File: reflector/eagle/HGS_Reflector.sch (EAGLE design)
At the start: 19 parts, among them J1 U.FL, U1 TQP3M9037, U2 TQP3M903X, U3 LP2985XX-N

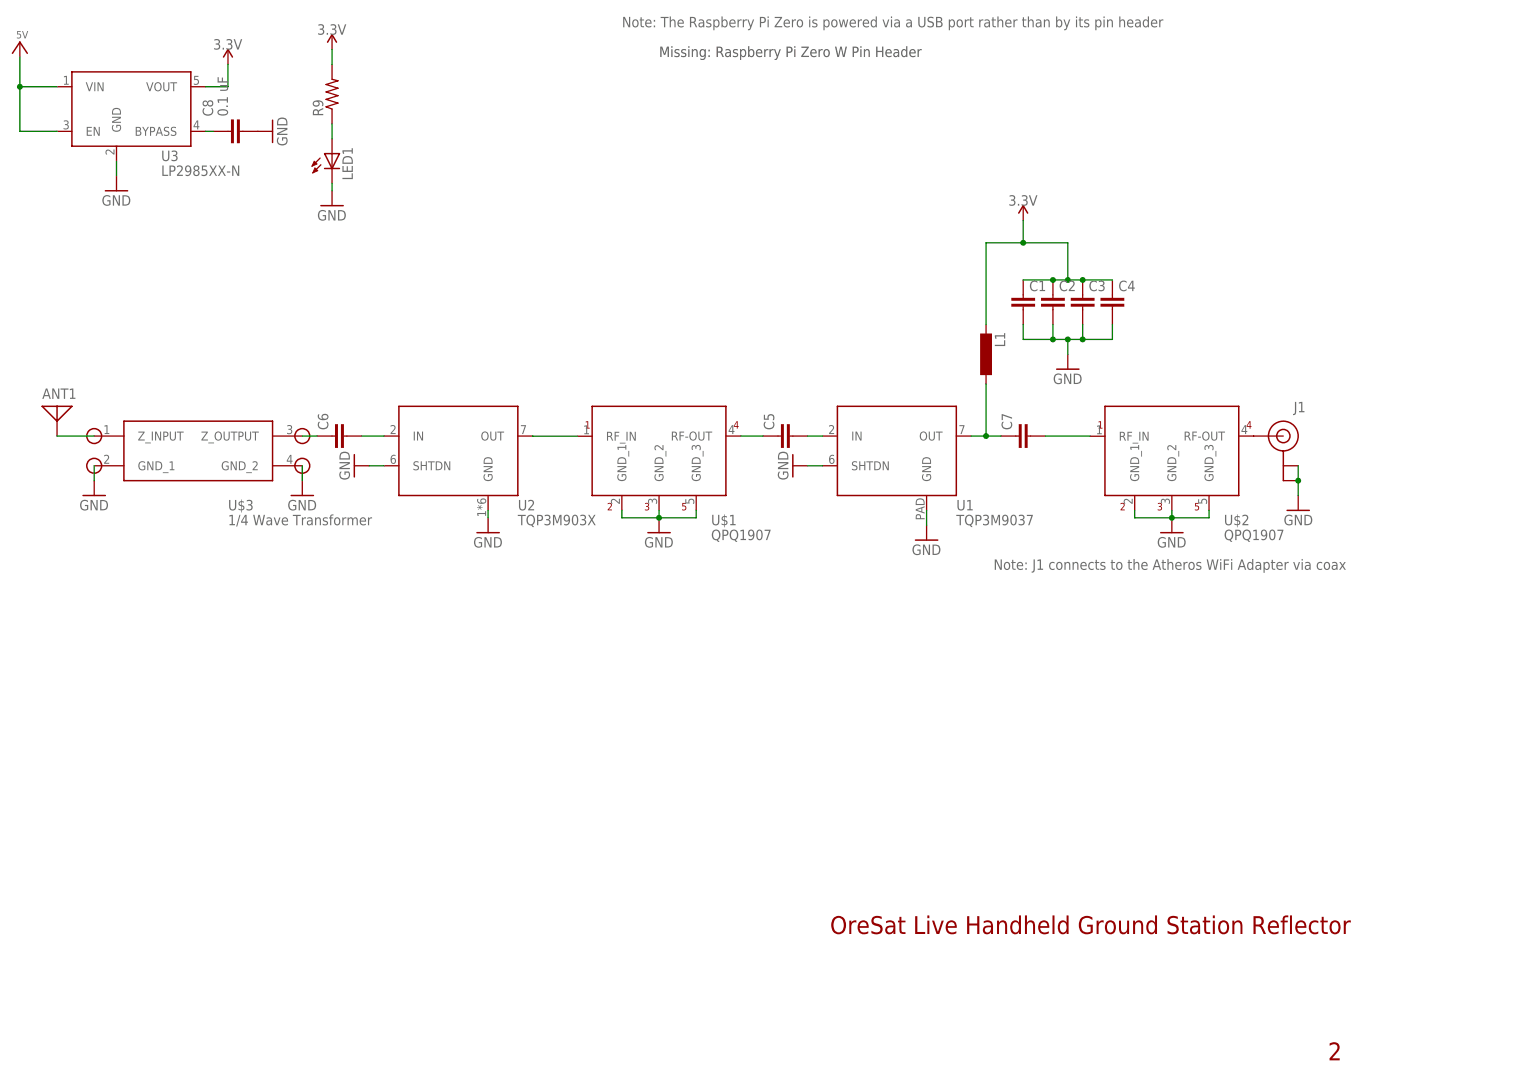
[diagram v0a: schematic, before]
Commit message: My EAGLE accidentally named something wrong, so I am fixing that.
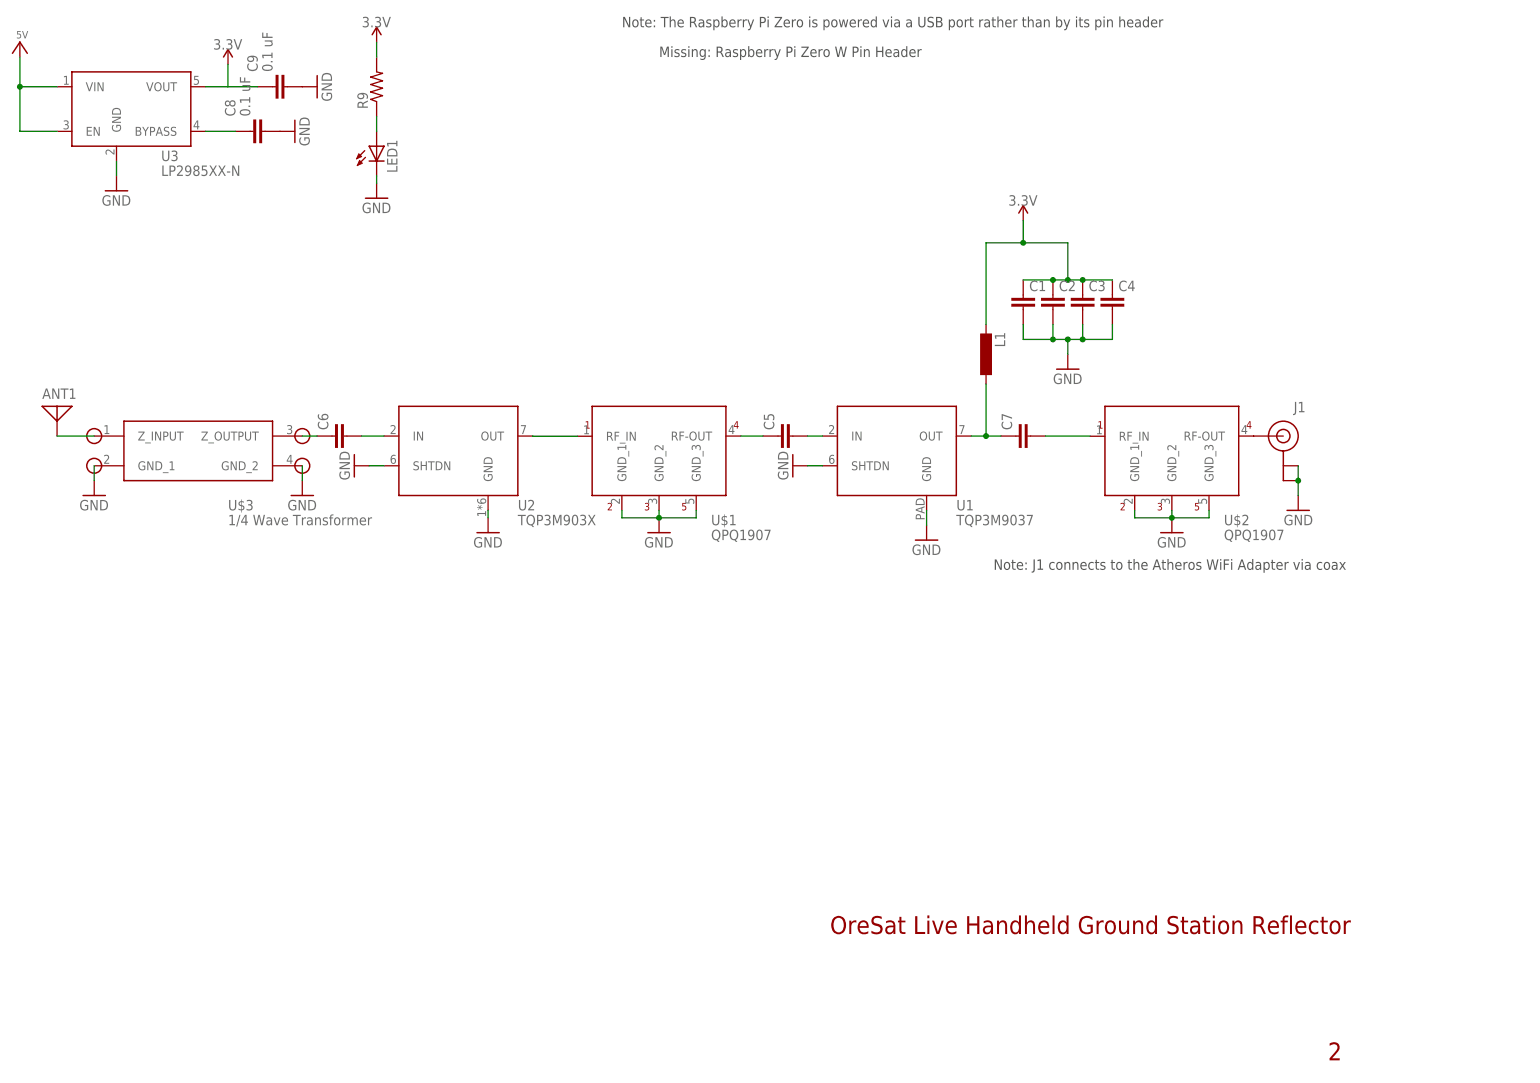
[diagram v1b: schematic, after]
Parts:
- added C9: 0.1 uF, ngspice-simulation:C
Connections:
- new net N$13: C9.1, U3.VOUT
- net 3.3V: no longer U3.VOUT
- net GND: now also C9.2
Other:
- moved on the sheet: C8, LED1, R9
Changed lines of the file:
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@@
 <part name="C8" library="ngspice-simulation" library_urn="urn:adsk.eagle:library:527439" deviceset="C" device="" value="0.1 uF"/>
 <part name="GND13" library="supply1" library_urn="urn:adsk.eagle:library:371" deviceset="GND" device=""/>
+<part name="C9" library="ngspice-simulation" library_urn="urn:adsk.eagle:library:527439" deviceset="C" device="" value="0.1 uF"/>
+<part name="GND14" library="supply1" library_urn="urn:adsk.eagle:library:371" deviceset="GND" device=""/>
 </parts>
 <sheets>
@@
 <text x="180.34" y="27.94" size="3.048" layer="94">OreSat Live Handheld Ground Station Reflector</text>
 <text x="265.43" y="6.35" size="3.048" layer="94">2</text>
-<text x="144.78" y="182.88" size="1.778" layer="95">Note: The Raspberry Pi Zero is powered via a USB port rather than by its pin header</text>
-<text x="208.28" y="90.17" size="1.778" layer="95">Note: J1 connects to the Atheros WiFi Adapter via coax</text>
+<text x="144.78" y="182.88" size="1.778" layer="97">Note: The Raspberry Pi Zero is powered via a USB port rather than by its pin header</text>
+<text x="208.28" y="90.17" size="1.778" layer="97">Note: J1 connects to the Atheros WiFi Adapter via coax</text>
 </plain>
 <instances>
@@
 <attribute name="VALUE" x="218.44" y="121.92" size="1.778" layer="96"/>
 </instance>
-<instance part="LED1" gate="G$1" x="95.25" y="161.29" smashed="yes">
-<attribute name="NAME" x="98.806" y="156.718" size="1.778" layer="95" rot="R90"/>
-<attribute name="VALUE" x="100.965" y="156.718" size="1.778" layer="96" rot="R90"/>
-</instance>
-<instance part="R9" gate="R" x="95.25" y="171.45" smashed="yes" rot="R90">
-<attribute name="NAME" x="93.7514" y="167.64" size="1.778" layer="95" rot="R90"/>
-<attribute name="VALUE" x="98.552" y="167.64" size="1.778" layer="96" rot="R90"/>
+<instance part="LED1" gate="G$1" x="102.87" y="162.56" smashed="yes">
+<attribute name="NAME" x="106.426" y="157.988" size="1.778" layer="95" rot="R90"/>
+<attribute name="VALUE" x="108.585" y="157.988" size="1.778" layer="96" rot="R90"/>
+</instance>
+<instance part="R9" gate="R" x="102.87" y="172.72" smashed="yes" rot="R90">
+<attribute name="NAME" x="101.3714" y="168.91" size="1.778" layer="95" rot="R90"/>
+<attribute name="VALUE" x="106.172" y="168.91" size="1.778" layer="96" rot="R90"/>
 </instance>
 <instance part="C1" gate="CE" x="213.36" y="137.16" smashed="yes">
@@
 <attribute name="VALUE" x="119.38" y="93.98" size="1.778" layer="96"/>
 </instance>
-<instance part="3.3V2" gate="G$1" x="95.25" y="181.61" smashed="yes">
-<attribute name="VALUE" x="92.71" y="181.61" size="1.778" layer="96"/>
-</instance>
-<instance part="GND6" gate="1" x="95.25" y="152.4" smashed="yes">
-<attribute name="VALUE" x="92.71" y="149.86" size="1.778" layer="96"/>
+<instance part="3.3V2" gate="G$1" x="102.87" y="182.88" smashed="yes">
+<attribute name="VALUE" x="100.33" y="182.88" size="1.778" layer="96"/>
+</instance>
+<instance part="GND6" gate="1" x="102.87" y="153.67" smashed="yes">
+<attribute name="VALUE" x="100.33" y="151.13" size="1.778" layer="96"/>
 </instance>
 <instance part="C6" gate="CE" x="95.25" y="113.03" smashed="yes" rot="R90">
@@
 <attribute name="VALUE" x="171.45" y="110.49" size="1.778" layer="96" rot="R270"/>
 </instance>
-<instance part="C8" gate="G$1" x="77.47" y="165.1" smashed="yes" rot="R90">
-<attribute name="NAME" x="74.93" y="167.64" size="1.778" layer="95" rot="R90"/>
-<attribute name="VALUE" x="77.47" y="167.64" size="1.778" layer="96" rot="R90"/>
-</instance>
-<instance part="GND13" gate="1" x="85.09" y="165.1" smashed="yes" rot="R90">
-<attribute name="VALUE" x="87.63" y="162.56" size="1.778" layer="96" rot="R90"/>
+<instance part="C8" gate="G$1" x="81.28" y="165.1" smashed="yes" rot="R90">
+<attribute name="NAME" x="78.74" y="167.64" size="1.778" layer="95" rot="R90"/>
+<attribute name="VALUE" x="81.28" y="167.64" size="1.778" layer="96" rot="R90"/>
+</instance>
+<instance part="GND13" gate="1" x="88.9" y="165.1" smashed="yes" rot="R90">
+<attribute name="VALUE" x="91.44" y="162.56" size="1.778" layer="96" rot="R90"/>
+</instance>
+<instance part="C9" gate="G$1" x="85.09" y="172.72" smashed="yes" rot="R90">
+<attribute name="NAME" x="82.55" y="175.26" size="1.778" layer="95" rot="R90"/>
+<attribute name="VALUE" x="85.09" y="175.26" size="1.778" layer="96" rot="R90"/>
+</instance>
+<instance part="GND14" gate="1" x="92.71" y="172.72" smashed="yes" rot="R90">
+<attribute name="VALUE" x="95.25" y="170.18" size="1.778" layer="96" rot="R90"/>
 </instance>
 </instances>
@@
 <pinref part="LED1" gate="G$1" pin="C"/>
 <pinref part="GND6" gate="1" pin="GND"/>
-<wire x1="95.25" y1="154.94" x2="95.25" y2="156.21" width="0.1524" layer="91"/>
+<wire x1="102.87" y1="156.21" x2="102.87" y2="157.48" width="0.1524" layer="91"/>
 </segment>
 <segment>
@@
 <pinref part="GND13" gate="1" pin="GND"/>
 </segment>
+<segment>
+<pinref part="C9" gate="G$1" pin="2"/>
+<pinref part="GND14" gate="1" pin="GND"/>
+</segment>
 </net>
 <net name="N$5" class="0">
@@
 <pinref part="LED1" gate="G$1" pin="A"/>
 <pinref part="R9" gate="R" pin="1"/>
-<wire x1="95.25" y1="166.37" x2="95.25" y2="163.83" width="0.1524" layer="91"/>
+<wire x1="102.87" y1="167.64" x2="102.87" y2="165.1" width="0.1524" layer="91"/>
 </segment>
 </net>
 <net name="3.3V" class="0">
-<segment>
-<pinref part="U3" gate="G$1" pin="VOUT"/>
-<pinref part="3.3V1" gate="G$1" pin="3.3V"/>
-<wire x1="73.66" y1="172.72" x2="77.47" y2="172.72" width="0.1524" layer="91"/>
-<wire x1="77.47" y1="172.72" x2="77.47" y2="176.53" width="0.1524" layer="91"/>
-</segment>
 <segment>
 <pinref part="R9" gate="R" pin="2"/>
 <pinref part="3.3V2" gate="G$1" pin="3.3V"/>
-<wire x1="95.25" y1="179.07" x2="95.25" y2="176.53" width="0.1524" layer="91"/>
+<wire x1="102.87" y1="180.34" x2="102.87" y2="177.8" width="0.1524" layer="91"/>
 </segment>
 <segment>
@@
 <pinref part="U3" gate="G$1" pin="BYPASS"/>
 <pinref part="C8" gate="G$1" pin="1"/>
-<wire x1="74.93" y1="165.1" x2="73.66" y2="165.1" width="0.1524" layer="91"/>
+<wire x1="78.74" y1="165.1" x2="73.66" y2="165.1" width="0.1524" layer="91"/>
 </segment>
 </net>
@@
 </segment>
 </net>
+<net name="N$13" class="0">
+<segment>
+<pinref part="C9" gate="G$1" pin="1"/>
+<wire x1="82.55" y1="172.72" x2="77.47" y2="172.72" width="0.1524" layer="91"/>
+<pinref part="U3" gate="G$1" pin="VOUT"/>
+<pinref part="3.3V1" gate="G$1" pin="3.3V"/>
+<wire x1="73.66" y1="172.72" x2="77.47" y2="172.72" width="0.1524" layer="91"/>
+<wire x1="77.47" y1="172.72" x2="77.47" y2="176.53" width="0.1524" layer="91"/>
+</segment>
+</net>
